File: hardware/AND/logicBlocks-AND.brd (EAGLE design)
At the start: 26.4 x 16.5 mm, 14 parts, among them U1 7408SE

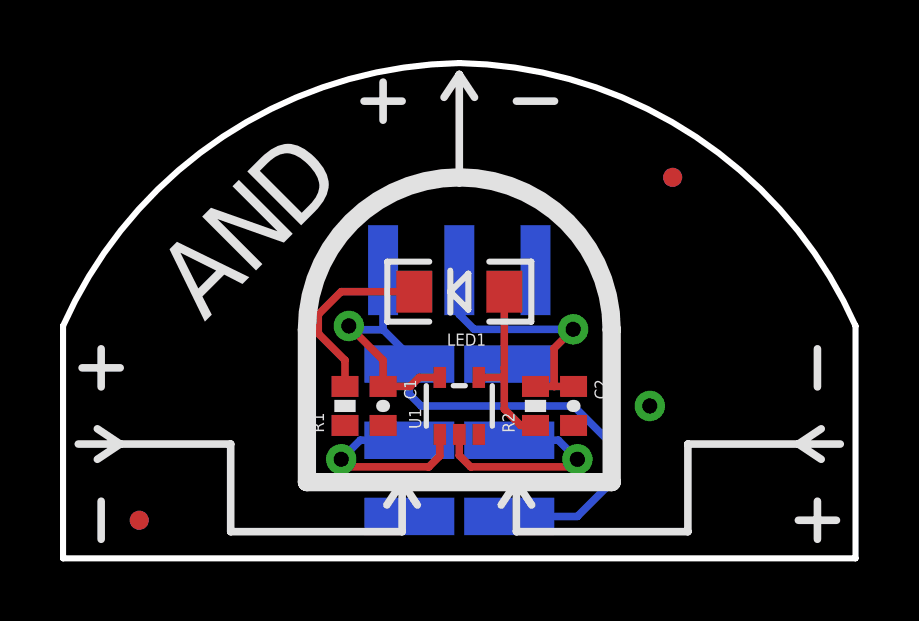
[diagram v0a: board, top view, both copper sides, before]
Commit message: v12 of all boards -- Male headers w/ posts
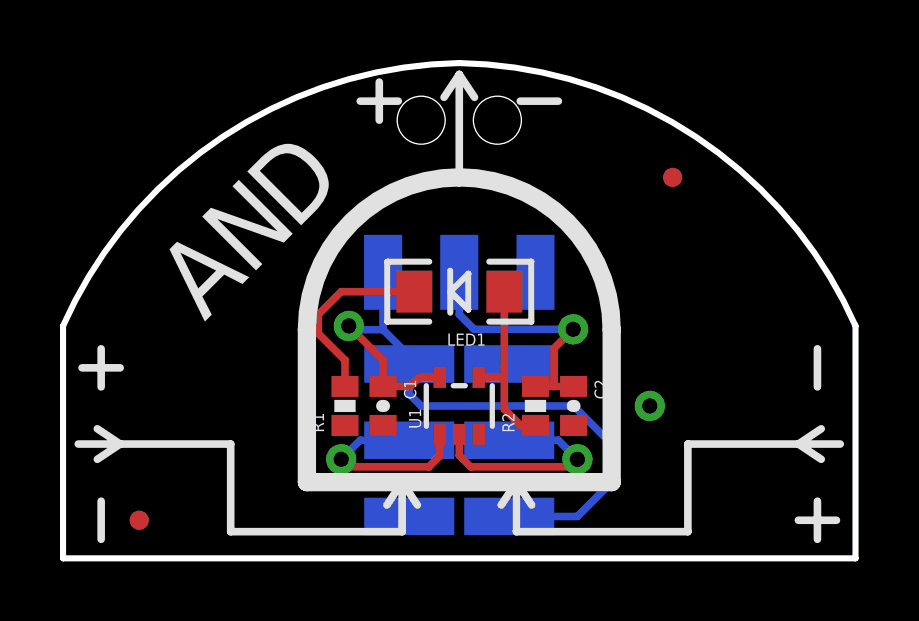
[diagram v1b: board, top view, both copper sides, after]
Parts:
- removed JP3: OUTPUT, SparkFun:1X03-SMD-MALE
- added JP9: OUTPUT, SparkFun-Connectors:1X03_SMD_RA_MALE_POST
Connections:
- net GND: now also JP9.3; no longer JP3.3
- net N$3: now also JP9.2; no longer JP3.2
- net VCC: now also JP9.1; no longer JP3.1
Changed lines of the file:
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@@
 <layer number="144" name="Drill_legend" color="7" fill="1" visible="no" active="yes"/>
 <layer number="151" name="HeatSink" color="7" fill="1" visible="no" active="yes"/>
+<layer number="199" name="Contour" color="7" fill="1" visible="no" active="yes"/>
 <layer number="200" name="200bmp" color="1" fill="10" visible="no" active="yes"/>
 <layer number="201" name="201bmp" color="2" fill="10" visible="no" active="yes"/>
@@
 <wire x1="25.146" y1="6.985" x2="25.146" y2="5.715" width="0.254" layer="21"/>
 <wire x1="24.511" y1="1.27" x2="25.781" y2="1.27" width="0.254" layer="21"/>
-<wire x1="11.303" y1="15.24" x2="10.033" y2="15.24" width="0.254" layer="21"/>
-<wire x1="16.383" y1="15.24" x2="15.113" y2="15.24" width="0.254" layer="21"/>
-<wire x1="10.668" y1="15.875" x2="10.668" y2="14.605" width="0.254" layer="21"/>
+<wire x1="11.176" y1="15.24" x2="9.906" y2="15.24" width="0.254" layer="21"/>
+<wire x1="16.51" y1="15.24" x2="15.24" y2="15.24" width="0.254" layer="21"/>
+<wire x1="10.541" y1="15.875" x2="10.541" y2="14.605" width="0.254" layer="21"/>
 <wire x1="8.128" y1="7.62" x2="13.208" y2="12.7" width="0.6096" layer="21" curve="-90"/>
 <wire x1="13.208" y1="12.7" x2="18.288" y2="7.62" width="0.6096" layer="21" curve="-90"/>
@@
 <param name="dpGapFactor" value="2.5"/>
 <param name="checkGrid" value="0"/>
-<param name="checkAngle" value="1"/>
+<param name="checkAngle" value="0"/>
 <param name="checkFont" value="1"/>
 <param name="checkRestrict" value="1"/>
@@
 <element name="JP1" library="SparkFun" package="1X03-SMD-FEMALE" value="INPUT" x="4.318" y="3.937" rot="MR90"/>
 <element name="JP2" library="SparkFun" package="1X03-SMD-FEMALE" value="INPUT" x="22.098" y="3.937" rot="MR270"/>
-<element name="JP3" library="SparkFun" package="1X03-SMD-MALE" value="OUTPUT" x="13.208" y="14.605" rot="MR180"/>
 <element name="U1" library="SparkFun" package="SOT353" value="7408SE" x="13.208" y="5.08"/>
 <element name="R1" library="SparkFun" package="0402-RES" value="200" x="9.398" y="5.08" rot="R90"/>
@@
 <element name="JP7" library="SparkFun" package="MICRO-FIDUCIAL" value="FIDUCIALUFIDUCIAL" x="2.54" y="1.27"/>
 <element name="JP8" library="SparkFun" package="MICRO-FIDUCIAL" value="FIDUCIALUFIDUCIAL" x="20.32" y="12.7"/>
+<element name="JP9" library="SparkFun-Connectors" package="1X03_SMD_RA_MALE_POST" value="OUTPUT" x="13.208" y="14.605" rot="MR180"/>
 </elements>
 <signals>
@@
 <contactref element="JP1" pad="6"/>
 <contactref element="JP2" pad="6"/>
-<contactref element="JP3" pad="3"/>
 <contactref element="U1" pad="3"/>
 <contactref element="R1" pad="1"/>
@@
 <vertex x="26.416" y="0"/>
 </polygon>
+<contactref element="JP9" pad="3"/>
 </signal>
 <signal name="VCC">
 <contactref element="JP1" pad="4"/>
 <contactref element="JP2" pad="4"/>
-<contactref element="JP3" pad="1"/>
 <contactref element="U1" pad="5"/>
 <contactref element="C1" pad="1"/>
@@
 <wire x1="10.668" y1="7.62" x2="9.652" y2="7.62" width="0.254" layer="16"/>
 <wire x1="9.652" y1="7.62" x2="9.525" y2="7.747" width="0.254" layer="16"/>
-<wire x1="10.668" y1="7.62" x2="10.668" y2="9.605" width="0.254" layer="16"/>
+<wire x1="10.668" y1="7.62" x2="10.668" y2="9.535" width="0.254" layer="16"/>
 <via x="9.525" y="7.747" extent="1-16" drill="0.508"/>
+<contactref element="JP9" pad="1"/>
 </signal>
 <signal name="N$1">
@@
 <contactref element="R2" pad="2"/>
 <contactref element="C2" pad="1"/>
-<contactref element="JP3" pad="2"/>
 <wire x1="16.368" y1="5.73" x2="15.748" y2="5.73" width="0.254" layer="1"/>
 <wire x1="13.701" y1="7.635" x2="17.003" y2="7.635" width="0.254" layer="16"/>
-<wire x1="13.208" y1="9.605" x2="13.208" y2="8.128" width="0.254" layer="16"/>
+<wire x1="13.208" y1="9.535" x2="13.208" y2="8.128" width="0.254" layer="16"/>
 <wire x1="13.208" y1="8.128" x2="13.701" y2="7.635" width="0.254" layer="16"/>
 <wire x1="16.368" y1="7" x2="16.368" y2="5.73" width="0.254" layer="1"/>
@@
 <wire x1="16.368" y1="5.73" x2="17.018" y2="5.73" width="0.254" layer="1"/>
 <via x="17.003" y="7.635" extent="1-16" drill="0.508"/>
+<contactref element="JP9" pad="2"/>
 </signal>
 </signals>
